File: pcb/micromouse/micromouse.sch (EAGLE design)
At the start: 70 parts, among them IC1 LM2575-5.0WU-(TR), IC2 LM2575-3.3WU-(TR), IC3 DSPIC33FJ64MC804-PT, IC4 L293D, Y1 7.3728MHz

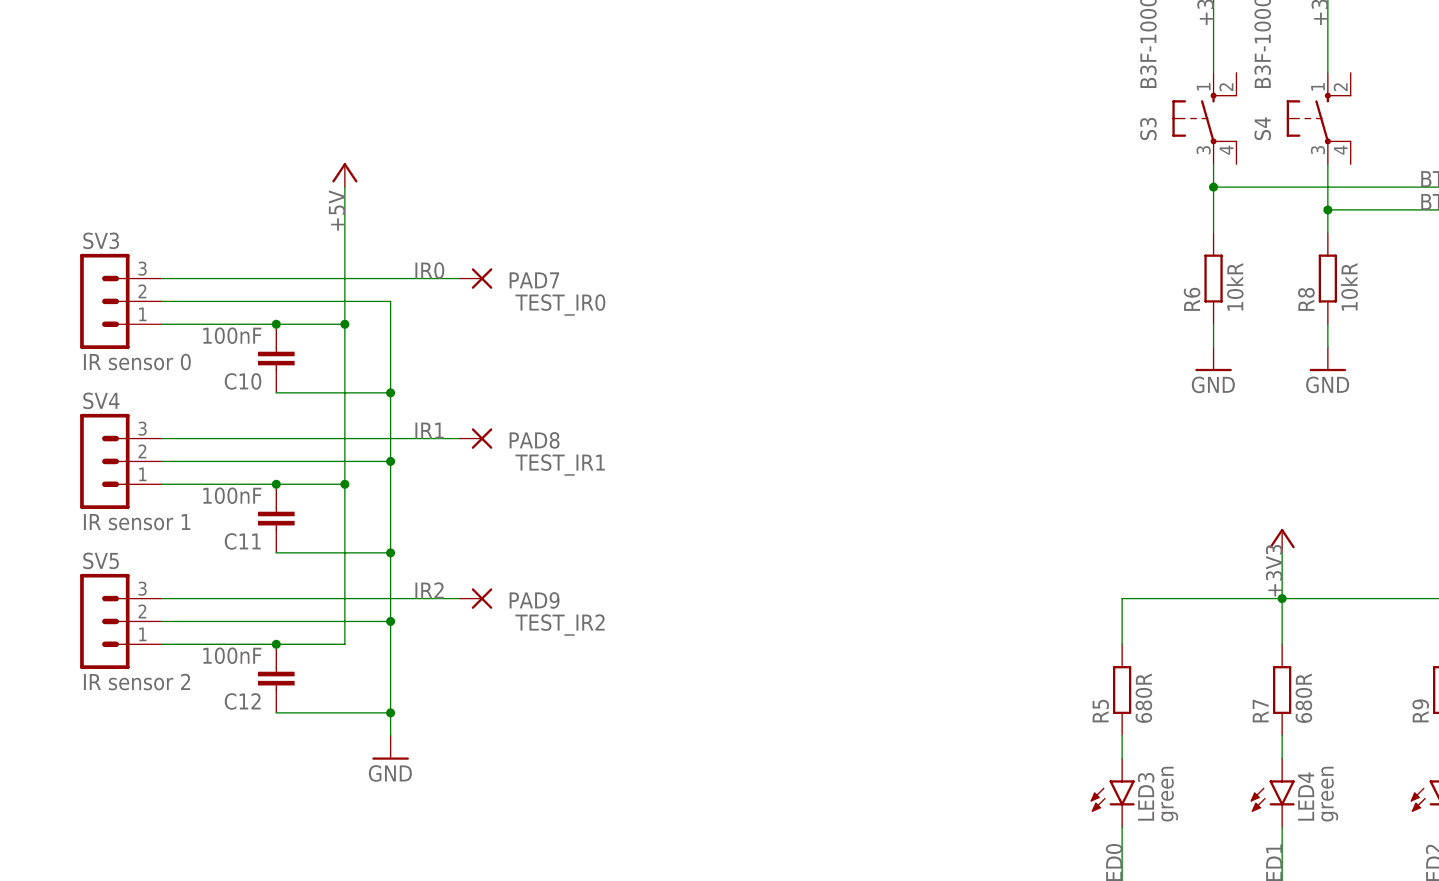
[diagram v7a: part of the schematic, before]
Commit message: Added low pass filter for distance sensors
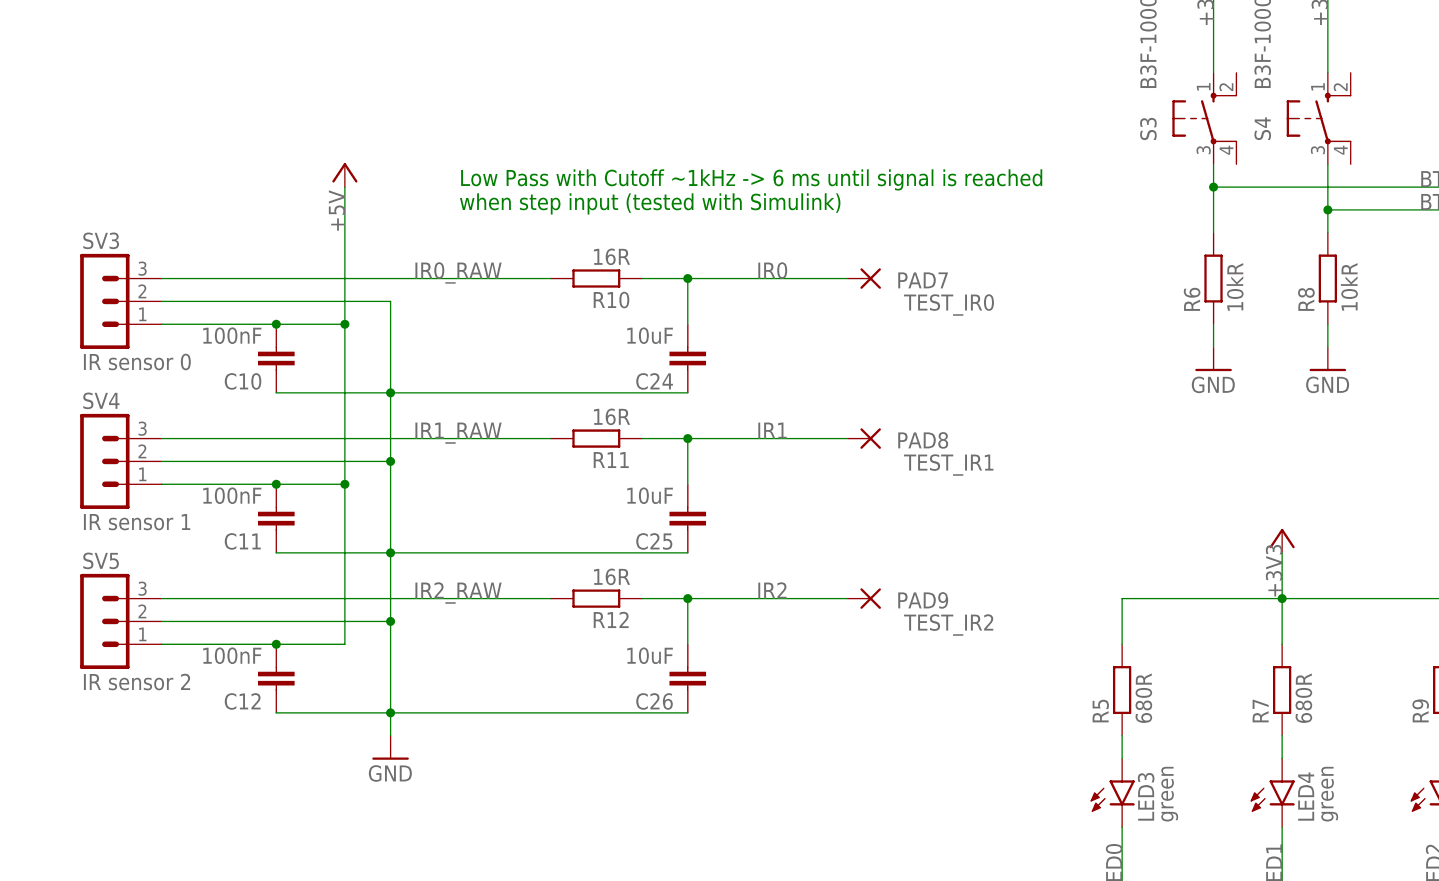
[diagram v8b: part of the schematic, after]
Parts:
- added C24, C25, C26: 10uF, rcl:C-EUC0805
- added R10, R11, R12: 16R, rcl:R-EU_R0805
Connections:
- new net IR0_RAW: R10.2, SV3.3
- new net IR1_RAW: R11.2, SV4.3
- new net IR2_RAW: R12.2, SV5.3
- net GND: now also C24.1, C25.1, C26.1
- net IR0: now also C24.2, R10.1; no longer SV3.3
- net IR1: now also C25.2, R11.1; no longer SV4.3
- net IR2: now also C26.2, R12.1; no longer SV5.3
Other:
- note added: "Low Pass with Cutoff ~1kHz -> 6 ms until signal is reached when step input (tested with Simulink)"
- moved on the sheet: PAD7, PAD8, PAD9
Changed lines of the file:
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@@
 <part name="C22" library="rcl" library_urn="urn:adsk.eagle:library:334" deviceset="C-EU" device="C0805" package3d_urn="urn:adsk.eagle:package:23617/2" value="100nF"/>
 <part name="C23" library="rcl" library_urn="urn:adsk.eagle:library:334" deviceset="C-EU" device="C0805" package3d_urn="urn:adsk.eagle:package:23617/2" value="100nF"/>
+<part name="R10" library="rcl" library_urn="urn:adsk.eagle:library:334" deviceset="R-EU_" device="R0805" package3d_urn="urn:adsk.eagle:package:23553/2" value="16R"/>
+<part name="R11" library="rcl" library_urn="urn:adsk.eagle:library:334" deviceset="R-EU_" device="R0805" package3d_urn="urn:adsk.eagle:package:23553/2" value="16R"/>
+<part name="R12" library="rcl" library_urn="urn:adsk.eagle:library:334" deviceset="R-EU_" device="R0805" package3d_urn="urn:adsk.eagle:package:23553/2" value="16R"/>
+<part name="C24" library="rcl" library_urn="urn:adsk.eagle:library:334" deviceset="C-EU" device="C0805" package3d_urn="urn:adsk.eagle:package:23617/2" value="10uF"/>
+<part name="C25" library="rcl" library_urn="urn:adsk.eagle:library:334" deviceset="C-EU" device="C0805" package3d_urn="urn:adsk.eagle:package:23617/2" value="10uF"/>
+<part name="C26" library="rcl" library_urn="urn:adsk.eagle:library:334" deviceset="C-EU" device="C0805" package3d_urn="urn:adsk.eagle:package:23617/2" value="10uF"/>
 </parts>
 <sheets>
@@
 <text x="8.89" y="115.062" size="1.778" layer="91">+</text>
 <text x="9.144" y="109.982" size="1.778" layer="91">Tantulum</text>
+<text x="144.78" y="317.5" size="1.778" layer="91">Low Pass with Cutoff ~1kHz -&gt; 6 ms until signal is reached
+when step input (tested with Simulink)</text>
 </plain>
 <instances>
@@
 <attribute name="VALUE" x="49.403" y="290.322" size="1.778" layer="96" rot="R180"/>
 </instance>
-<instance part="PAD7" gate="1" x="147.32" y="309.88" smashed="yes" rot="R180">
-<attribute name="NAME" x="156.083" y="310.5658" size="1.778" layer="95" rot="R180"/>
-<attribute name="VALUE" x="161.163" y="308.102" size="1.778" layer="96" rot="R180"/>
-</instance>
-<instance part="PAD8" gate="1" x="147.32" y="292.1" smashed="yes" rot="R180">
-<attribute name="NAME" x="156.083" y="292.7858" size="1.778" layer="95" rot="R180"/>
-<attribute name="VALUE" x="161.163" y="290.322" size="1.778" layer="96" rot="R180"/>
-</instance>
-<instance part="PAD9" gate="1" x="147.32" y="274.32" smashed="yes" rot="R180">
-<attribute name="NAME" x="156.083" y="275.0058" size="1.778" layer="95" rot="R180"/>
-<attribute name="VALUE" x="161.163" y="272.542" size="1.778" layer="96" rot="R180"/>
+<instance part="PAD7" gate="1" x="190.5" y="309.88" smashed="yes" rot="R180">
+<attribute name="NAME" x="199.263" y="310.5658" size="1.778" layer="95" rot="R180"/>
+<attribute name="VALUE" x="204.343" y="308.102" size="1.778" layer="96" rot="R180"/>
+</instance>
+<instance part="PAD8" gate="1" x="190.5" y="292.1" smashed="yes" rot="R180">
+<attribute name="NAME" x="199.263" y="292.7858" size="1.778" layer="95" rot="R180"/>
+<attribute name="VALUE" x="204.343" y="290.322" size="1.778" layer="96" rot="R180"/>
+</instance>
+<instance part="PAD9" gate="1" x="190.5" y="274.32" smashed="yes" rot="R180">
+<attribute name="NAME" x="199.263" y="275.0058" size="1.778" layer="95" rot="R180"/>
+<attribute name="VALUE" x="204.343" y="272.542" size="1.778" layer="96" rot="R180"/>
 </instance>
 <instance part="PAD10" gate="1" x="154.94" y="66.04" smashed="yes" rot="R180">
@@
 <attribute name="NAME" x="-49.784" y="276.479" size="1.778" layer="95" rot="R180"/>
 <attribute name="VALUE" x="-49.784" y="281.559" size="1.778" layer="96" rot="R180"/>
+</instance>
+<instance part="R10" gate="G$1" x="160.02" y="309.88" smashed="yes" rot="R180">
+<attribute name="NAME" x="163.83" y="308.3814" size="1.778" layer="95" rot="R180"/>
+<attribute name="VALUE" x="163.83" y="313.182" size="1.778" layer="96" rot="R180"/>
+</instance>
+<instance part="R11" gate="G$1" x="160.02" y="292.1" smashed="yes" rot="R180">
+<attribute name="NAME" x="163.83" y="290.6014" size="1.778" layer="95" rot="R180"/>
+<attribute name="VALUE" x="163.83" y="295.402" size="1.778" layer="96" rot="R180"/>
+</instance>
+<instance part="R12" gate="G$1" x="160.02" y="274.32" smashed="yes" rot="R180">
+<attribute name="NAME" x="163.83" y="272.8214" size="1.778" layer="95" rot="R180"/>
+<attribute name="VALUE" x="163.83" y="277.622" size="1.778" layer="96" rot="R180"/>
+</instance>
+<instance part="C24" gate="G$1" x="170.18" y="299.72" smashed="yes" rot="R180">
+<attribute name="NAME" x="168.656" y="299.339" size="1.778" layer="95" rot="R180"/>
+<attribute name="VALUE" x="168.656" y="304.419" size="1.778" layer="96" rot="R180"/>
+</instance>
+<instance part="C25" gate="G$1" x="170.18" y="281.94" smashed="yes" rot="R180">
+<attribute name="NAME" x="168.656" y="281.559" size="1.778" layer="95" rot="R180"/>
+<attribute name="VALUE" x="168.656" y="286.639" size="1.778" layer="96" rot="R180"/>
+</instance>
+<instance part="C26" gate="G$1" x="170.18" y="264.16" smashed="yes" rot="R180">
+<attribute name="NAME" x="168.656" y="263.779" size="1.778" layer="95" rot="R180"/>
+<attribute name="VALUE" x="168.656" y="268.859" size="1.778" layer="96" rot="R180"/>
 </instance>
 </instances>
@@
 <wire x1="124.46" y1="279.4" x2="137.16" y2="279.4" width="0.1524" layer="91"/>
 <junction x="137.16" y="279.4"/>
+<pinref part="C24" gate="G$1" pin="1"/>
+<wire x1="137.16" y1="297.18" x2="170.18" y2="297.18" width="0.1524" layer="91"/>
+<pinref part="C25" gate="G$1" pin="1"/>
+<wire x1="137.16" y1="279.4" x2="170.18" y2="279.4" width="0.1524" layer="91"/>
+<pinref part="C26" gate="G$1" pin="1"/>
+<wire x1="137.16" y1="261.62" x2="170.18" y2="261.62" width="0.1524" layer="91"/>
 </segment>
 <segment>
@@
 </segment>
 <segment>
-<pinref part="SV5" gate="G$1" pin="3"/>
-<wire x1="111.76" y1="274.32" x2="144.78" y2="274.32" width="0.1524" layer="91"/>
-<label x="139.7" y="274.32" size="1.778" layer="95"/>
+<pinref part="R12" gate="G$1" pin="1"/>
+<pinref part="C26" gate="G$1" pin="2"/>
+<wire x1="165.1" y1="274.32" x2="170.18" y2="274.32" width="0.1524" layer="91"/>
+<wire x1="170.18" y1="274.32" x2="170.18" y2="269.24" width="0.1524" layer="91"/>
 <pinref part="PAD9" gate="1" pin="P"/>
+<wire x1="170.18" y1="274.32" x2="187.96" y2="274.32" width="0.1524" layer="91"/>
+<junction x="170.18" y="274.32"/>
+<label x="177.8" y="274.32" size="1.778" layer="95"/>
 </segment>
 </net>
@@
 </segment>
 <segment>
-<pinref part="SV3" gate="G$1" pin="3"/>
-<wire x1="111.76" y1="309.88" x2="144.78" y2="309.88" width="0.1524" layer="91"/>
-<label x="139.7" y="309.88" size="1.778" layer="95"/>
+<pinref part="R10" gate="G$1" pin="1"/>
 <pinref part="PAD7" gate="1" pin="P"/>
+<wire x1="165.1" y1="309.88" x2="170.18" y2="309.88" width="0.1524" layer="91"/>
+<pinref part="C24" gate="G$1" pin="2"/>
+<wire x1="170.18" y1="309.88" x2="187.96" y2="309.88" width="0.1524" layer="91"/>
+<wire x1="170.18" y1="304.8" x2="170.18" y2="309.88" width="0.1524" layer="91"/>
+<junction x="170.18" y="309.88"/>
+<label x="177.8" y="309.88" size="1.778" layer="95"/>
 </segment>
 </net>
@@
 </segment>
 <segment>
-<pinref part="SV4" gate="G$1" pin="3"/>
-<wire x1="111.76" y1="292.1" x2="144.78" y2="292.1" width="0.1524" layer="91"/>
-<label x="139.7" y="292.1" size="1.778" layer="95"/>
+<pinref part="R11" gate="G$1" pin="1"/>
 <pinref part="PAD8" gate="1" pin="P"/>
+<wire x1="165.1" y1="292.1" x2="170.18" y2="292.1" width="0.1524" layer="91"/>
+<pinref part="C25" gate="G$1" pin="2"/>
+<wire x1="170.18" y1="292.1" x2="187.96" y2="292.1" width="0.1524" layer="91"/>
+<wire x1="170.18" y1="287.02" x2="170.18" y2="292.1" width="0.1524" layer="91"/>
+<junction x="170.18" y="292.1"/>
+<label x="177.8" y="292.1" size="1.778" layer="95"/>
 </segment>
 </net>
@@
 </segment>
 </net>
+<net name="IR0_RAW" class="0">
+<segment>
+<pinref part="SV3" gate="G$1" pin="3"/>
+<pinref part="R10" gate="G$1" pin="2"/>
+<wire x1="111.76" y1="309.88" x2="154.94" y2="309.88" width="0.1524" layer="91"/>
+<label x="139.7" y="309.88" size="1.778" layer="95"/>
+</segment>
+</net>
+<net name="IR1_RAW" class="0">
+<segment>
+<pinref part="SV4" gate="G$1" pin="3"/>
+<pinref part="R11" gate="G$1" pin="2"/>
+<wire x1="111.76" y1="292.1" x2="154.94" y2="292.1" width="0.1524" layer="91"/>
+<label x="139.7" y="292.1" size="1.778" layer="95"/>
+</segment>
+</net>
+<net name="IR2_RAW" class="0">
+<segment>
+<pinref part="SV5" gate="G$1" pin="3"/>
+<pinref part="R12" gate="G$1" pin="2"/>
+<wire x1="111.76" y1="274.32" x2="154.94" y2="274.32" width="0.1524" layer="91"/>
+<label x="139.7" y="274.32" size="1.778" layer="95"/>
+</segment>
+</net>
